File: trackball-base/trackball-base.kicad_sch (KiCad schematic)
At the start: 0 parts

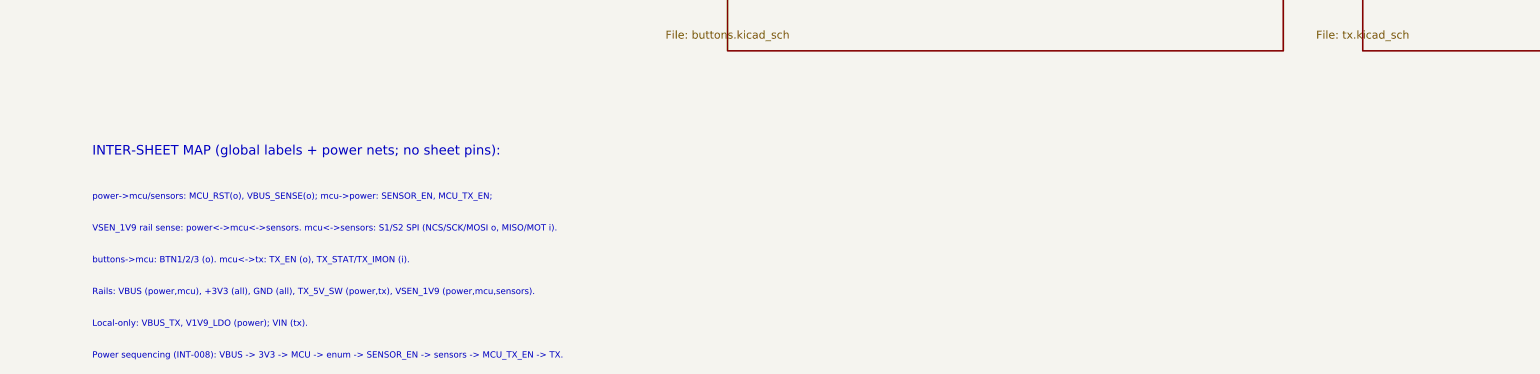
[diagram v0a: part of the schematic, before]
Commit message: layout: placed+silk+parity-0 (drc10: 0 errors/0 parity, 125 warnings)
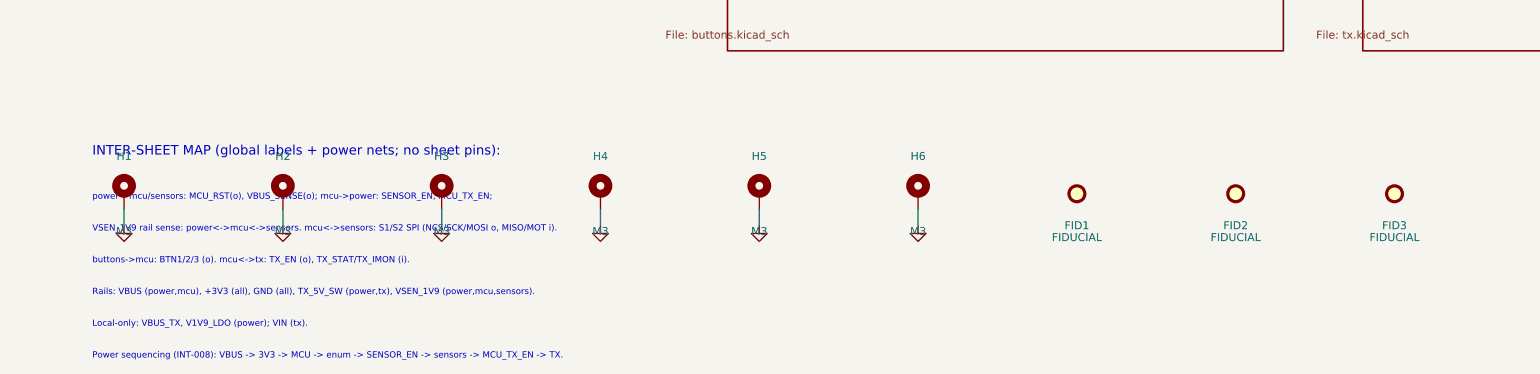
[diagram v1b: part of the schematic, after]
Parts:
- added FID1, FID2, FID3: FIDUCIAL, Fiducial:Fiducial_1mm_Mask2mm, symbol Mechanical:Fiducial
- added H1, H2, H3, H4, H5, H6: M3, MountingHole:MountingHole_3.2mm_M3_Pad, symbol Mechanical:MountingHole_Pad
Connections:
- new net GND: H1.1, H2.1, H3.1, H4.1, H5.1, H6.1
